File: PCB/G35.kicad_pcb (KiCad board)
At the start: 2 copper layers, 140.3 x 119.1 mm, 116 parts, among them J1 USB_C_Receptacle_USB2.0-Reduc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, K0:0 MX_1U, K0:1 MX_1U, K0:2 MX_1U, K0:3 MX_1U, K0:4 MX_1U, K0:5 MX_1U, K0:6 MX_1U, K1:0 MX_1U, K1:1 MX_1U, K1:2 MX_1U, K1:3 MX_1U, K1:4 MX_1U, K1:5 MX_1U, K1:6 MX_1U, K2:0 MX_1U, K2:1 MX_1U, K2:2 MX_1U, K2:3 MX_1U, K2:4 MX_1U, K2:5 MX_1U, K2:6 MX_1U, K3:0 MX_1U, K3:1 MX_1U, K3:2 MX_1U, K3:3 MX_1U, K3:4 MX_1U, K3:5 MX_1U, K3:6 MX_1U, K4:0 MX_1U, K4:1 MX_1U, K4:2 MX_1.5U, K4:3 MX_1.25U, K4:4 MX_1.5U, K4:5 MX_1.75U, K4:6 MX_1.75U, K4:62 MX_1.75U, M1 Conn_01x01, M2 Conn_01x01, M3 Conn_01x01, M4 Conn_01x01, M5 Conn_01x01, M6 Conn_01x01, M7 Conn_01x01, SW1 SW_Push, U1 ATmega32U4-AU, U2 PRTR5V0U2X, Y1 16MHz

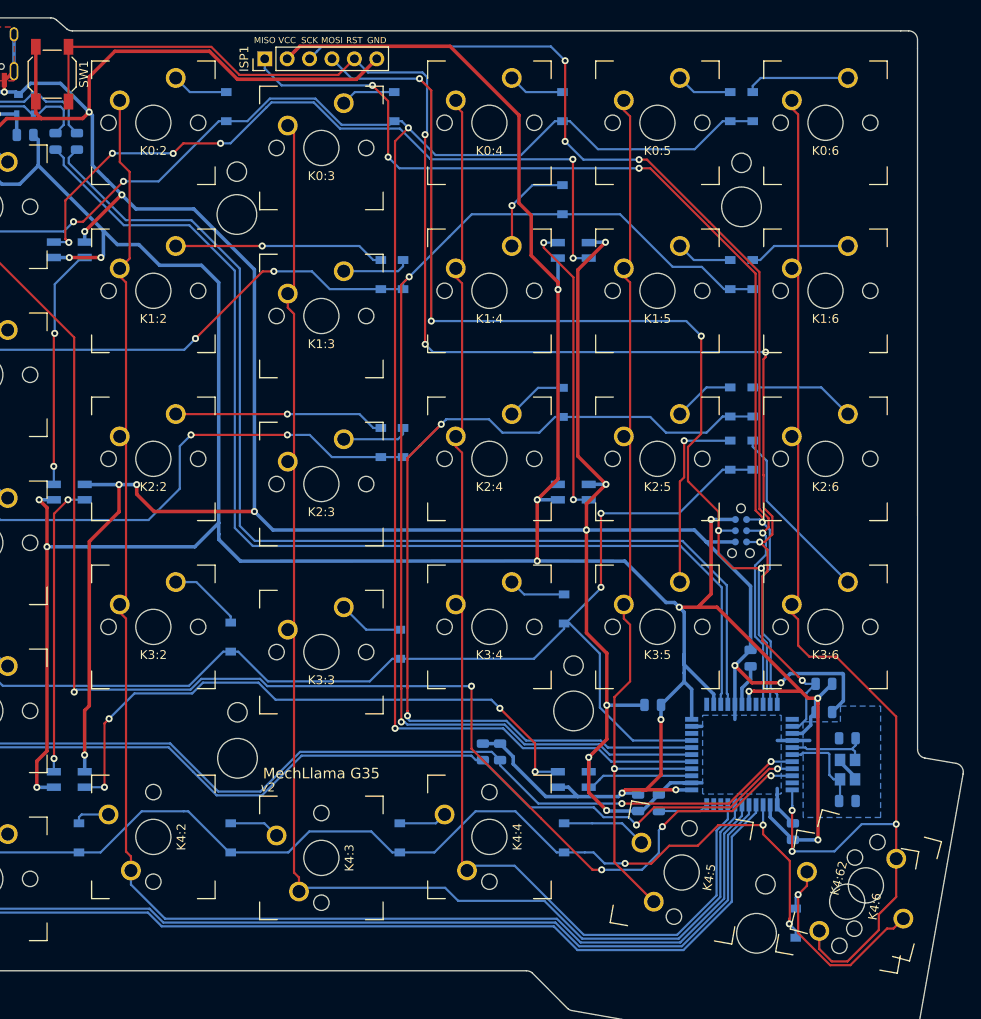
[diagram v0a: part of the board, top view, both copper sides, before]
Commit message: Initial cleanup fixes
Remove extra thumb key footprint
Cleanup widths of main GND and +5V traces
Combine ground zone for crystal and mcu
Move 1x6 ISP header closer to mcu
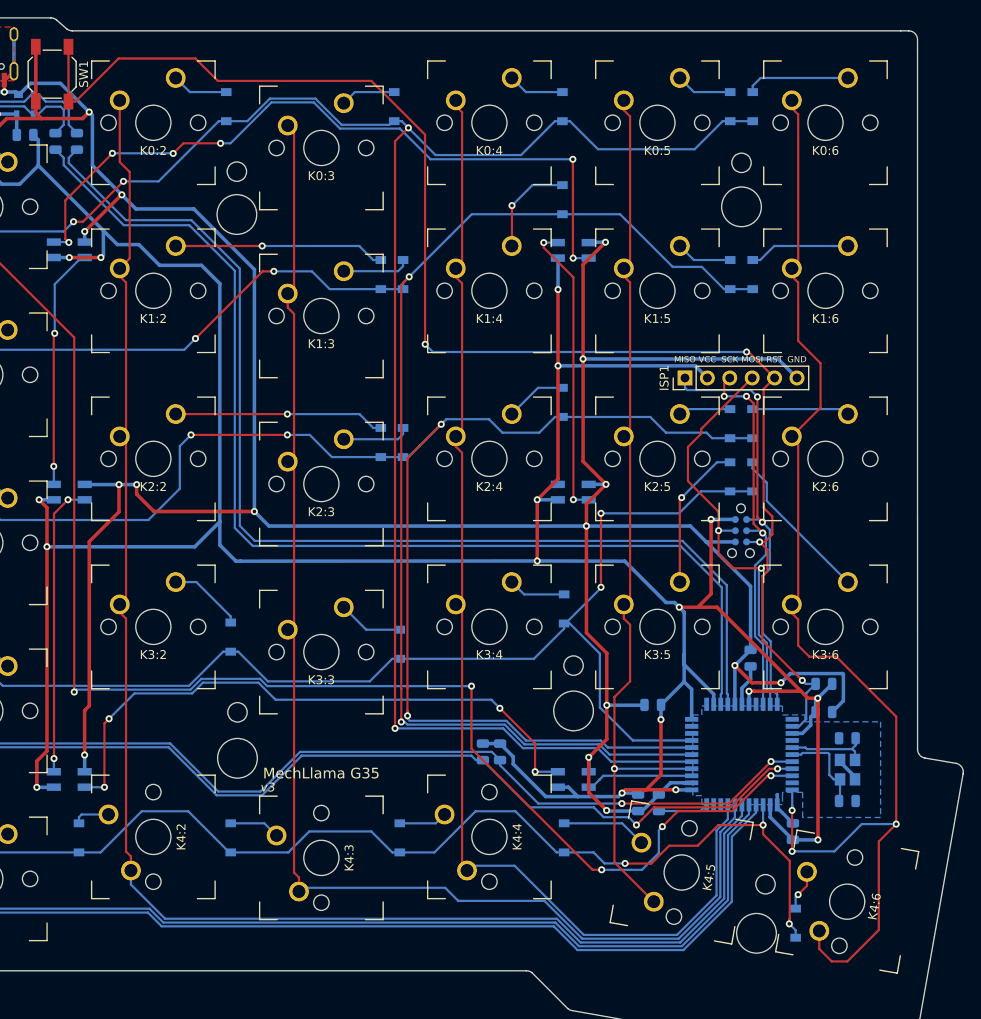
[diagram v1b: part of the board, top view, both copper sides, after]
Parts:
- removed K4:62: MX_1.75U, MX_Only:MXOnly-1.75U-NoLED
- moved ISP1 59.8 mm to (186.1, 77.1)
- moved D2:5 2.46 mm to (191.2, 82.3)
- moved D2:6 2.46 mm to (193.7, 82.3)
- moved D3:5 2.46 mm to (191.2, 88.3)
- moved D3:6 2.46 mm to (193.7, 88.3)
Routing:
- net SCK: track 120.2 -> 43.5 mm, vias 4 -> 3
- net MISO: track 122.5 -> 48.1 mm, vias 4 -> 2
- net MOSI: track 120.5 -> 47.9 mm, vias 5 -> 2
- net +5V: track 451.5 -> 417.8 mm, vias 17 -> 18
- net GND: track 455.2 -> 431.3 mm, vias 18 -> 19
- net Net-(D4:6-Pad2): track 24.7 -> 4.70 mm
- net Net-(D3:5-Pad2): track 21.5 -> 16.8 mm
- net RESET: track 169.8 -> 165.4 mm, vias 5 -> 4
- net col6: track 134.3 -> 137.4 mm
- net Net-(D3:6-Pad2): track 20.5 -> 18.1 mm
- net Net-(D2:5-Pad2): track 6.96 -> 5.92 mm
- net row3: track 141.6 -> 140.5 mm
- net Net-(D2:6-Pad2): track 12.0 -> 11.0 mm
- net row2: track 181.5 -> 181.0 mm
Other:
- board text added: "v3"
- board text removed: "v2"

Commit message: stage
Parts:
- removed B1: Buzzer, MechLlama:Buzzer_SMD_KLJ-1102_11x9
- removed ISP1: AVR-ISP-6-PIN, MechLlama:PinHeader_1x06_P2.54mm_Vertical_ISP
- removed ISP2: AVR-ISP-6-TAG, MechLlama:Tag-Connect_TC2030-IDC-NL_2x03_P1.27mm_Vertical
- removed OLED1: SSD1306, MechLlama:PinHeader_SSD1306
- removed RGB1, RGB2, RGB3, RGB4, RGB5, RGB6: WS2812, MechLlama:LED_WS-2812B-Mini
- removed Y1: 16MHz, Crystal:Crystal_SMD_3225-4Pin_3.2x2.5mm
- added C10: 0.1uF, Capacitor_SMD:C_0805_2012Metric, F.Cu at (40.6, 41.0)
- added C11: 0.1uF, Capacitor_SMD:C_0805_2012Metric, F.Cu at (27.4, 46.9)
- added C12: 0.1uF, Capacitor_SMD:C_0805_2012Metric, F.Cu at (50.9, 29.7)
- added C13: 0.1uF, Capacitor_SMD:C_0805_2012Metric, F.Cu at (46.0, 34.3)
- added C14: 4.7uF, Capacitor_SMD:C_0805_2012Metric, F.Cu at (37.4, 46.1)
- added C15: 1uF, Capacitor_SMD:C_0805_2012Metric, F.Cu at (23.0, 46.9)
- added C16: 1uF, Capacitor_SMD:C_0805_2012Metric, F.Cu at (46.0, 37.4)
- added C17: 0.1uF, Capacitor_SMD:C_0805_2012Metric, F.Cu at (50.9, 32.7)
- added C18: 0.01uF, Capacitor_SMD:C_0805_2012Metric, F.Cu at (45.0, 41.0)
- added C19: 1uF, Capacitor_SMD:C_0805_2012Metric, F.Cu at (55.3, 29.7)
- added C20: 4.7nF, Capacitor_SMD:C_0805_2012Metric, F.Cu at (41.8, 44.1)
- added C21: 0.1uF, Capacitor_SMD:C_0805_2012Metric, F.Cu at (50.5, 35.7)
- added C8: 0.47uF, Capacitor_SMD:C_0805_2012Metric, F.Cu at (90.7, 12.6)
- added C9: 1uF, Capacitor_SMD:C_0805_2012Metric, F.Cu at (55.3, 32.7)
- added D1: LED_ABRG, MechLlama:LED_Wurth_150141M173100, F.Cu at (48.1, 17.7)
- added D10: LED_ABRG, MechLlama:LED_Wurth_150141M173100, F.Cu at (48.1, 22.1)
- added D11: LED_ABRG, MechLlama:LED_Wurth_150141M173100, F.Cu at (54.1, 17.7)
- added D12: LED_ABRG, MechLlama:LED_Wurth_150141M173100, F.Cu at (60.2, 13.3)
- added D13: LED_ABRG, MechLlama:LED_Wurth_150141M173100, F.Cu at (54.1, 22.1)
- added D14: LED_ABRG, MechLlama:LED_Wurth_150141M173100, F.Cu at (60.2, 17.7)
- added D15: LED_ABRG, MechLlama:LED_Wurth_150141M173100, F.Cu at (29.9, 13.3)
- added D16: LED_ABRG, MechLlama:LED_Wurth_150141M173100, F.Cu at (23.8, 4.53)
- added D17: LED_ABRG, MechLlama:LED_Wurth_150141M173100, F.Cu at (29.9, 0.14)
- added D18: LED_ABRG, MechLlama:LED_Wurth_150141M173100, F.Cu at (23.8, 8.92)
- added D19: LED_ABRG, MechLlama:LED_Wurth_150141M173100, F.Cu at (29.9, 4.53)
- added D2: LED_ABRG, MechLlama:LED_Wurth_150141M173100, F.Cu at (42.0, 22.1)
- added D20: LED_ABRG, MechLlama:LED_Wurth_150141M173100, F.Cu at (36.0, 0.14)
- added D21: LED_ABRG, MechLlama:LED_Wurth_150141M173100, F.Cu at (23.8, 13.3)
- added D22: LED_ABRG, MechLlama:LED_Wurth_150141M173100, F.Cu at (29.9, 8.92)
- added D23: LED_ABRG, MechLlama:LED_Wurth_150141M173100, F.Cu at (60.2, 8.92)
- added D24: LED_ABRG, MechLlama:LED_Wurth_150141M173100, F.Cu at (42.0, 0.14)
- added D25: LED_ABRG, MechLlama:LED_Wurth_150141M173100, F.Cu at (23.8, 17.7)
- added D26: LED_ABRG, MechLlama:LED_Wurth_150141M173100, F.Cu at (23.8, 0.14)
- added D27: LED_ABRG, MechLlama:LED_Wurth_150141M173100, F.Cu at (36.0, 8.92)
- added D28: LED_ABRG, MechLlama:LED_Wurth_150141M173100, F.Cu at (42.0, 4.53)
- added D29: LED_ABRG, MechLlama:LED_Wurth_150141M173100, F.Cu at (23.8, 22.1)
- added D3: LED_ABRG, MechLlama:LED_Wurth_150141M173100, F.Cu at (54.1, 0.14)
- added D30: LED_ABRG, MechLlama:LED_Wurth_150141M173100, F.Cu at (48.1, 0.14)
- added D31: LED_ABRG, MechLlama:LED_Wurth_150141M173100, F.Cu at (29.9, 17.7)
- added D32: LED_ABRG, MechLlama:LED_Wurth_150141M173100, F.Cu at (36.0, 13.3)
- added D33: LED_ABRG, MechLlama:LED_Wurth_150141M173100, F.Cu at (42.0, 8.92)
- added D34: LED_ABRG, MechLlama:LED_Wurth_150141M173100, F.Cu at (48.1, 4.53)
- added D35: LED_ABRG, MechLlama:LED_Wurth_150141M173100, F.Cu at (29.9, 22.1)
- added D36: LED_ABRG, MechLlama:LED_Wurth_150141M173100, F.Cu at (54.1, 13.3)
- added D37: LED_ABRG, MechLlama:LED_Wurth_150141M173100, F.Cu at (60.2, 4.53)
- added D38: LED_ABRG, MechLlama:LED_Wurth_150141M173100, F.Cu at (36.0, 17.7)
- added D39: LED_ABRG, MechLlama:LED_Wurth_150141M173100, F.Cu at (42.0, 13.3)
- added D4: LED_ABRG, MechLlama:LED_Wurth_150141M173100, F.Cu at (54.1, 8.92)
- added D40: LED_ABRG, MechLlama:LED_Wurth_150141M173100, F.Cu at (48.1, 8.92)
- added D41: LED_ABRG, MechLlama:LED_Wurth_150141M173100, F.Cu at (54.1, 4.53)
- added D5: LED_ABRG, MechLlama:LED_Wurth_150141M173100, F.Cu at (48.1, 13.3)
- added D6: LED_ABRG, MechLlama:LED_Wurth_150141M173100, F.Cu at (42.0, 17.7)
- added D7: LED_ABRG, MechLlama:LED_Wurth_150141M173100, F.Cu at (60.2, 0.14)
- added D8: LED_ABRG, MechLlama:LED_Wurth_150141M173100, F.Cu at (36.0, 22.1)
- added D9: LED_ABRG, MechLlama:LED_Wurth_150141M173100, F.Cu at (36.0, 4.53)
- added J2: USB_C_Receptacle_USB2.0, Connector_USB:USB_C_Receptacle_HRO_TYPE-C-31-M-12, F.Cu at (105.7, 39.2)
- added J3: STM32_SWD, Connector:Tag-Connect_TC2030-IDC-NL_2x03_P1.27mm_Vertical, F.Cu at (34.3, 42.1)
- added R10: R, Resistor_SMD:R_0805_2012Metric, F.Cu at (49.5, 40.3)
- added R11: R, Resistor_SMD:R_0805_2012Metric, F.Cu at (41.8, 47.0)
- added R9: 10k, Resistor_SMD:R_0805_2012Metric, F.Cu at (46.3, 44.0)
- added U3: TLV70033_SOT23-5, Package_TO_SOT_SMD:SOT-23-5, F.Cu at (32.7, 46.9)
- added U4: STM32F070CBTx, Package_QFP:LQFP-48_7x7mm_P0.5mm, F.Cu at (38.1, 33.9)
- added U5: USBLC6-2SC6, Package_TO_SOT_SMD:SOT-23-6, F.Cu at (46.2, 30.5)
- C1: value 1uF -> 22uF; footprint Capacitor_SMD:C_0805_2012Metric -> Capacitor_SMD:CP_Elec_5x3.9; moved to F.Cu
- C2, C3, C4: value 0.1uF -> 0.47uF; moved to F.Cu
- C5, F1: moved to F.Cu
- C6, C7: value 22pF -> 0.1uF; moved to F.Cu
- J1: value USB_C_Receptacle_USB2.0-ReducedPins -> Case; footprint MechLlama:USB_C_Receptacle_HRO_TYPE-C-31-M-12 -> Connector_PinHeader_2.54mm:PinHeader_1x01_P2.54mm_Vertical
- K0:0, K0:1, K0:2, K0:3, K0:4, K0:5, K0:6, K1:0, K1:1, K1:2, K1:3, K1:4, K1:5, K1:6, K2:0, K2:1, K2:2, K2:3, K2:4, K2:5, K2:6, K3:0, K3:1, K3:2, K3:3, K3:4, K3:5, K3:6, K4:0, K4:1: value MX_1U -> 1U; footprint MX_Only:MXOnly-1U-NoLED -> keyswitches.pretty:SW_PG1350
- K4:2, K4:4: value MX_1.5U -> 1.5U; footprint MX_Only:MXOnly-1.5U-NoLED -> keyswitches.pretty:SW_PG1350_1.5u
- K4:3: value MX_1.25U -> 1.25U; footprint MX_Only:MXOnly-1.25U-NoLED -> keyswitches.pretty:SW_PG1350_rotatable
- K4:5, K4:6: value MX_1.75U -> 1.75U; footprint MX_Only:MXOnly-1.75U-NoLED -> keyswitches.pretty:SW_PG1350_1.5u
- R1, R2: value 5.1k -> I2C; moved to F.Cu
- R3: value 10k -> 100k; moved to F.Cu
- R4: value 4.7k -> 100k; moved to F.Cu
- R5: value 4.7k -> RSET; moved to F.Cu
- R6, R7: value 22 -> 5.1k; moved to F.Cu
- R8: value 10k -> 1M; moved to F.Cu
- U1: value ATmega32U4-AU -> OLED_SSD1306; footprint Package_QFP:TQFP-44_10x10mm_P0.8mm -> MechLlama:PinHeader_SSD1306; moved to F.Cu
- U2: value PRTR5V0U2X -> IS31FL3737; footprint MechLlama:SOT-143B -> Package_DFN_QFN:QFN-40-1EP_5x5mm_P0.4mm_EP3.8x3.8mm_ThermalVias; moved to F.Cu
- moved R8 165.4 mm to (54.9, 35.7), turned to 0 degrees
- moved C6 153.8 mm to (99.6, 12.6)
- moved C7 151.9 mm to (95.1, 12.6), turned to 0 degrees
- moved C1 150.2 mm to (76.7, 14.5), turned to 0 degrees
- moved C2 150.0 mm to (99.6, 15.6), turned to 0 degrees
- moved C3 147.1 mm to (90.7, 18.6)
- moved C4 139.1 mm to (95.1, 15.6), turned to 0 degrees
- moved R3 135.5 mm to (99.5, 18.5), turned to 0 degrees
- moved U1 135.3 mm to (79.3, 45.8), turned to 180 degrees
- moved C5 134.7 mm to (90.7, 15.6), turned to 0 degrees
- moved R4 123.2 mm to (104.0, 12.5), turned to 0 degrees
- moved R5 121.7 mm to (95.1, 18.5), turned to 0 degrees
- moved R7 71.0 mm to (46.2, 47.0), turned to 0 degrees
- moved R6 61.9 mm to (53.9, 38.7), turned to 0 degrees
- moved F1 60.9 mm to (50.7, 43.3), turned to 0 degrees
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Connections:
- C1 pad 1: /UCAP -> +5V
- C6 pad 1: XTAL1 -> +5V
- C7 pad 1: XTAL2 -> +5V
- F1 pad 2: VCC -> VBUS
- R1 pad 1: GND -> /LED & OLED/SCL
- R1 pad 2: Net-(J1-PadA5) -> +3V3
- R2 pad 1: GND -> +3V3
- R2 pad 2: Net-(J1-PadB5) -> /LED & OLED/SDA
- R3 pad 1: GND -> Net-(R3-Pad1)
- R3 pad 2: Net-(R3-Pad2) -> +3V3
- R4 pad 1: +5V -> Net-(R4-Pad1)
- R4 pad 2: SCL -> GND
- R5 pad 1: +5V -> Net-(R5-Pad1)
- R5 pad 2: SDA -> GND
- R6 pad 1: D- -> Net-(J2-PadA5)
- R6 pad 2: /DR- -> GND
- R7 pad 1: D+ -> GND
- R7 pad 2: /DR+ -> Net-(J2-PadB5)
- R8 pad 1: +5V -> /MCU, USB, & Power/SHIELD
- R8 pad 2: RESET -> GND
- SW1 pad 1: RESET -> /MCU, USB, & Power/BOOT0
- SW1 pad 2: GND -> +3V3
- U1 pad 1: (no net) -> GND
- U1 pad 2: +5V -> +3V3
- U1 pad 3: D- -> /LED & OLED/SCL
- U1 pad 4: D+ -> /LED & OLED/SDA
- U2 pad 1: GND -> /LED & OLED/RGB Matrix/SW1
- U2 pad 2: /DR+ -> /LED & OLED/RGB Matrix/SW2
- U2 pad 3: /DR- -> /LED & OLED/RGB Matrix/SW3
- U2 pad 4: VCC -> GND
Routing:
- net GND: track 431.3 -> 0.00 mm, vias 19 -> 0
- net +5V: track 417.8 -> 0.00 mm, vias 18 -> 0
- net row0: track 219.9 -> 0.00 mm, vias 4 -> 0
- net col0: track 207.1 -> 0.00 mm
- net SDA: track 205.1 -> 0.00 mm, vias 3 -> 0
- net row1: track 198.0 -> 0.00 mm, vias 4 -> 0
- net SCL: track 197.3 -> 0.00 mm, vias 4 -> 0
- net BUZZER: track 190.6 -> 0.00 mm, vias 7 -> 0
- net col1: track 187.1 -> 0.00 mm
- net row2: track 181.0 -> 0.00 mm, vias 4 -> 0
- net col2: track 175.0 -> 0.00 mm
- net RESET: track 165.4 -> 0.00 mm, vias 4 -> 0
- net col3: track 152.6 -> 0.00 mm
- net row3: track 140.5 -> 0.00 mm, vias 2 -> 0
- net col6: track 137.4 -> 0.00 mm, vias 3 -> 0
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- removed copper zone on B.Cu, net GND

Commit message: update edge cuts
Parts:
- K4:3: value 1.25U -> 1U
- K4:5, K4:6: value 1.75U -> 1.5U
- moved U4 30.5 mm to (60.6, 54.4)
- moved C1 11.7 mm to (75.9, 2.80)
- moved K4:6 8.20 mm to (204.4, 128.3)
- moved K4:0 8.20 mm to (87.7, 125.7)
- moved K4:1 8.20 mm to (106.7, 125.7)
- moved K4:3 8.20 mm to (144.8, 123.3)
- moved K4:5 8.20 mm to (185.7, 125.0)
- moved K4:2 7.96 mm to (125.8, 121.2)
- moved K4:4 7.96 mm to (163.9, 121.2)
- moved K3:3 6.15 mm to (144.8, 102.0)
- moved K3:0 6.15 mm to (87.7, 108.7)
- moved K3:1 6.15 mm to (106.7, 108.7)
- moved K3:2 6.15 mm to (125.8, 99.2)
- moved K3:4 6.15 mm to (163.9, 99.2)
- moved K3:5 6.15 mm to (182.9, 99.2)
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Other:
- board size 140.3 x 119.1 mm -> 139.5 x 108.7 mm
